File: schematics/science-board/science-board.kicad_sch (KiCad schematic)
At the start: 16 parts, among them J1 Conn_01x02, J10 Conn_01x04, J2 Conn_01x08, J3 Conn_01x04, J4 Conn_01x04, J5 Conn_01x08, J6 Conn_01x03, J7 Conn_01x08, J8 Conn_01x08, J9 Conn_01x04, U1 Teensy4.1, U2 LSF0108PWR

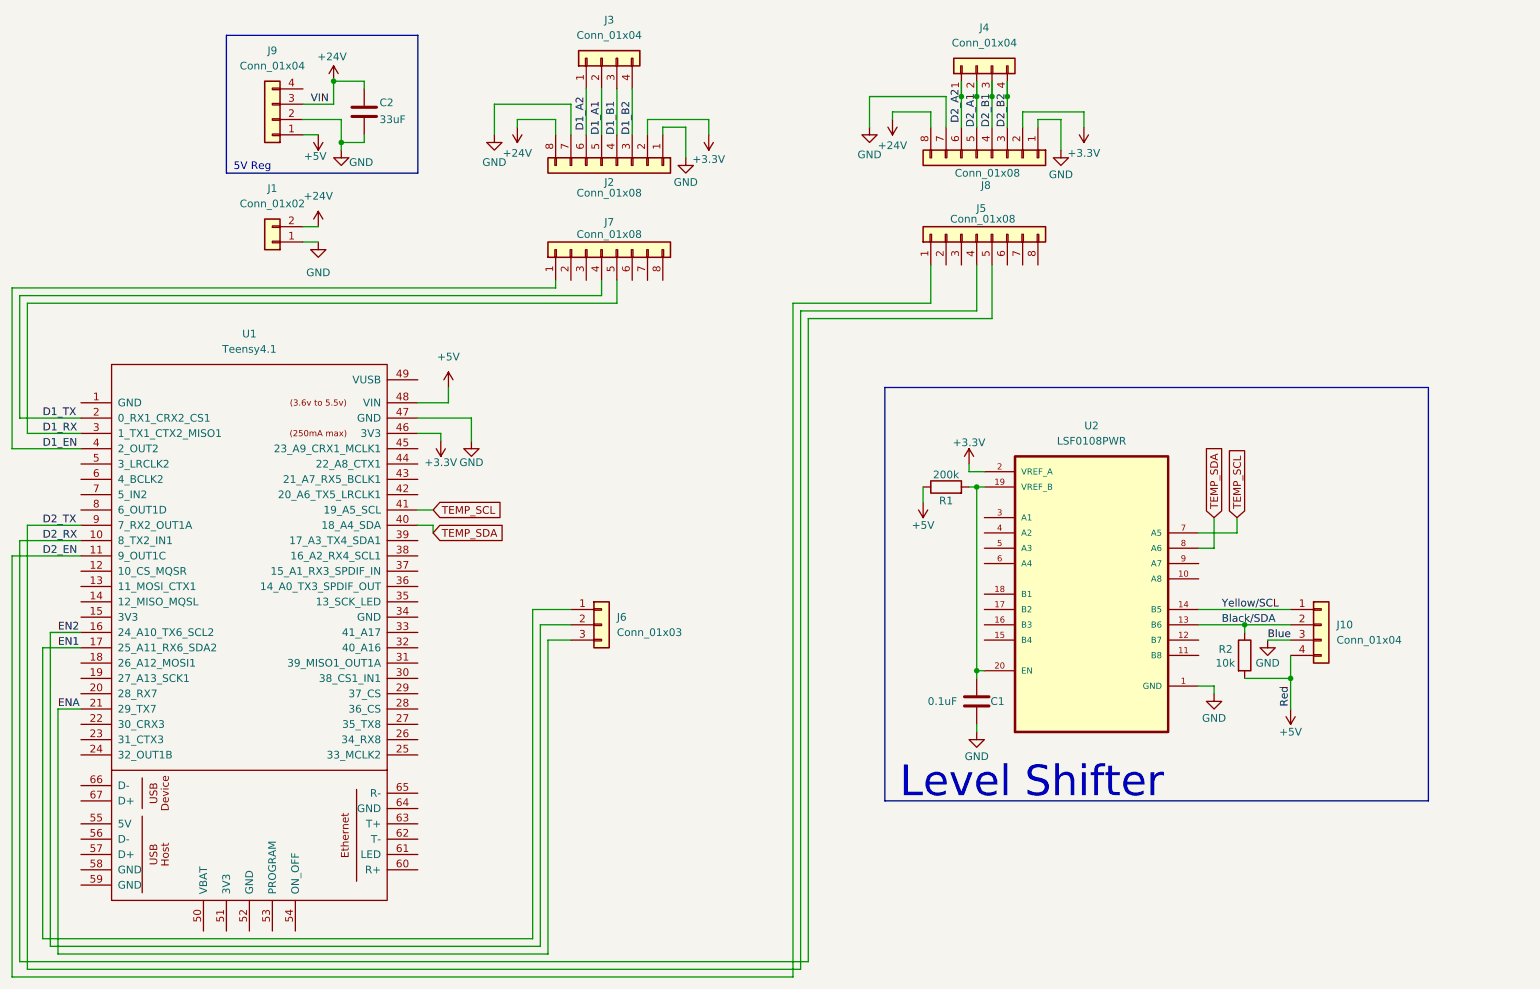
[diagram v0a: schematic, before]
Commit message: Finished preliminary routing. Used through-hole footprints.
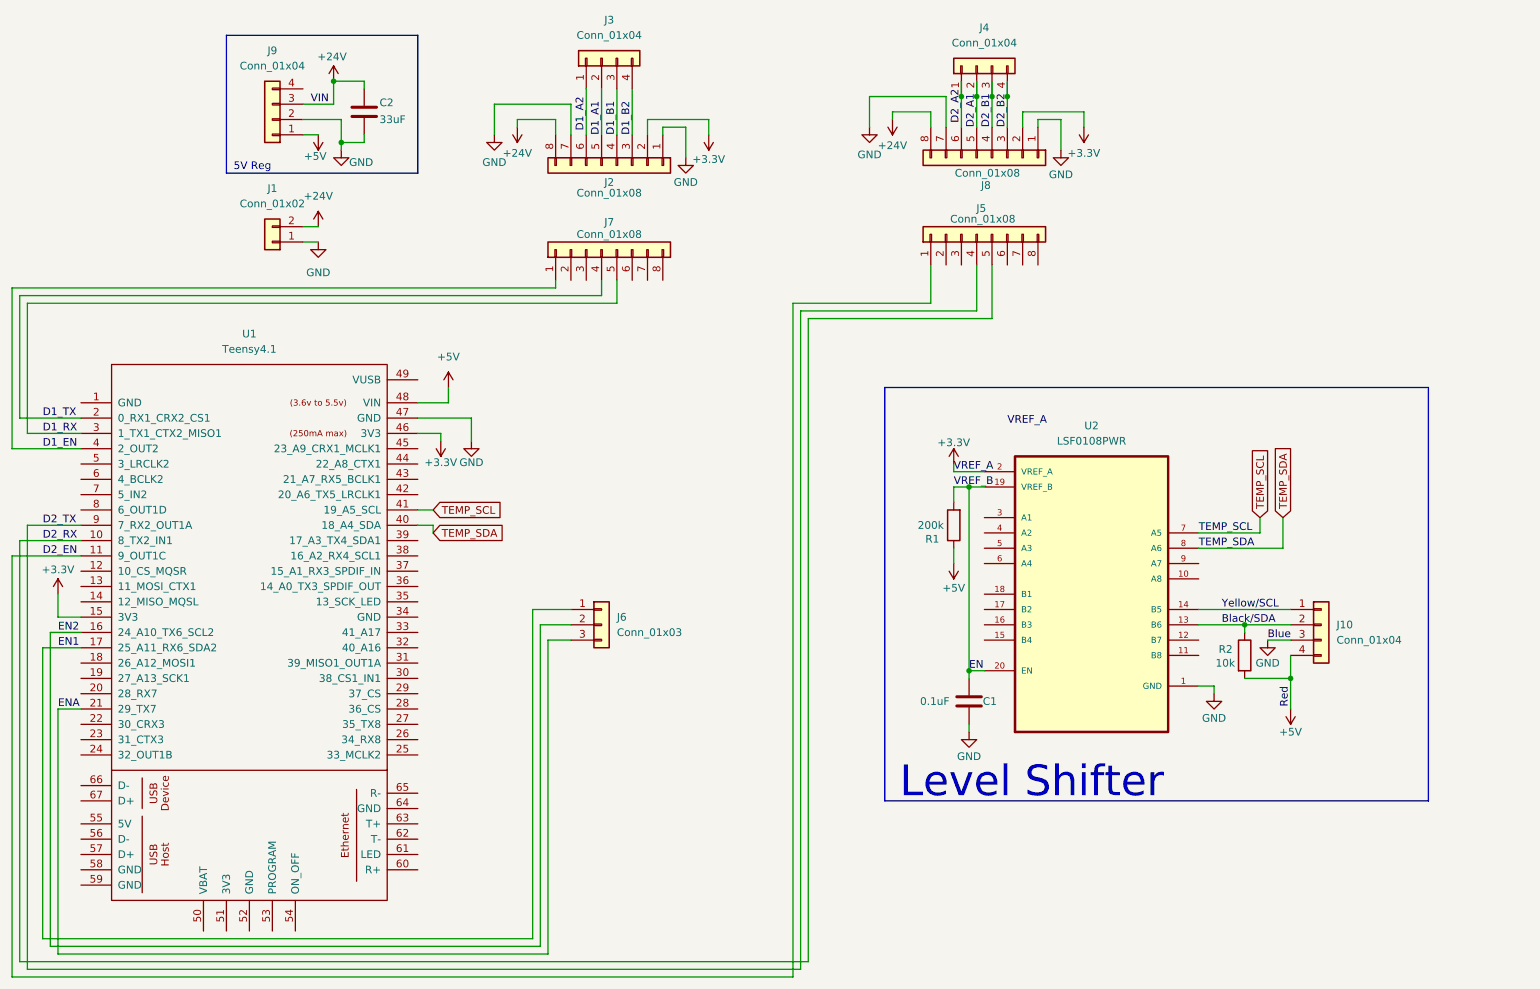
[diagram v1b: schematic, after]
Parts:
- C1: footprint Capacitor_SMD:C_0603_1608Metric -> Capacitor_THT:C_Disc_D3.0mm_W1.6mm_P2.50mm
- C2: footprint Capacitor_SMD:C_0805_2012Metric -> Capacitor_THT:CP_Radial_D4.0mm_P1.50mm
- R1, R2: footprint Resistor_SMD:R_0603_1608Metric -> Resistor_THT:R_Axial_DIN0204_L3.6mm_D1.6mm_P5.08mm_Horizontal
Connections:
- net +3.3V: now also U1.15 (3V3)
- net EN: now reaches C1.1, R1.2, U2.19 (VREF_B), U2.20 (EN)
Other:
- moved on the sheet: C1, R1

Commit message: Added Ethernet module.
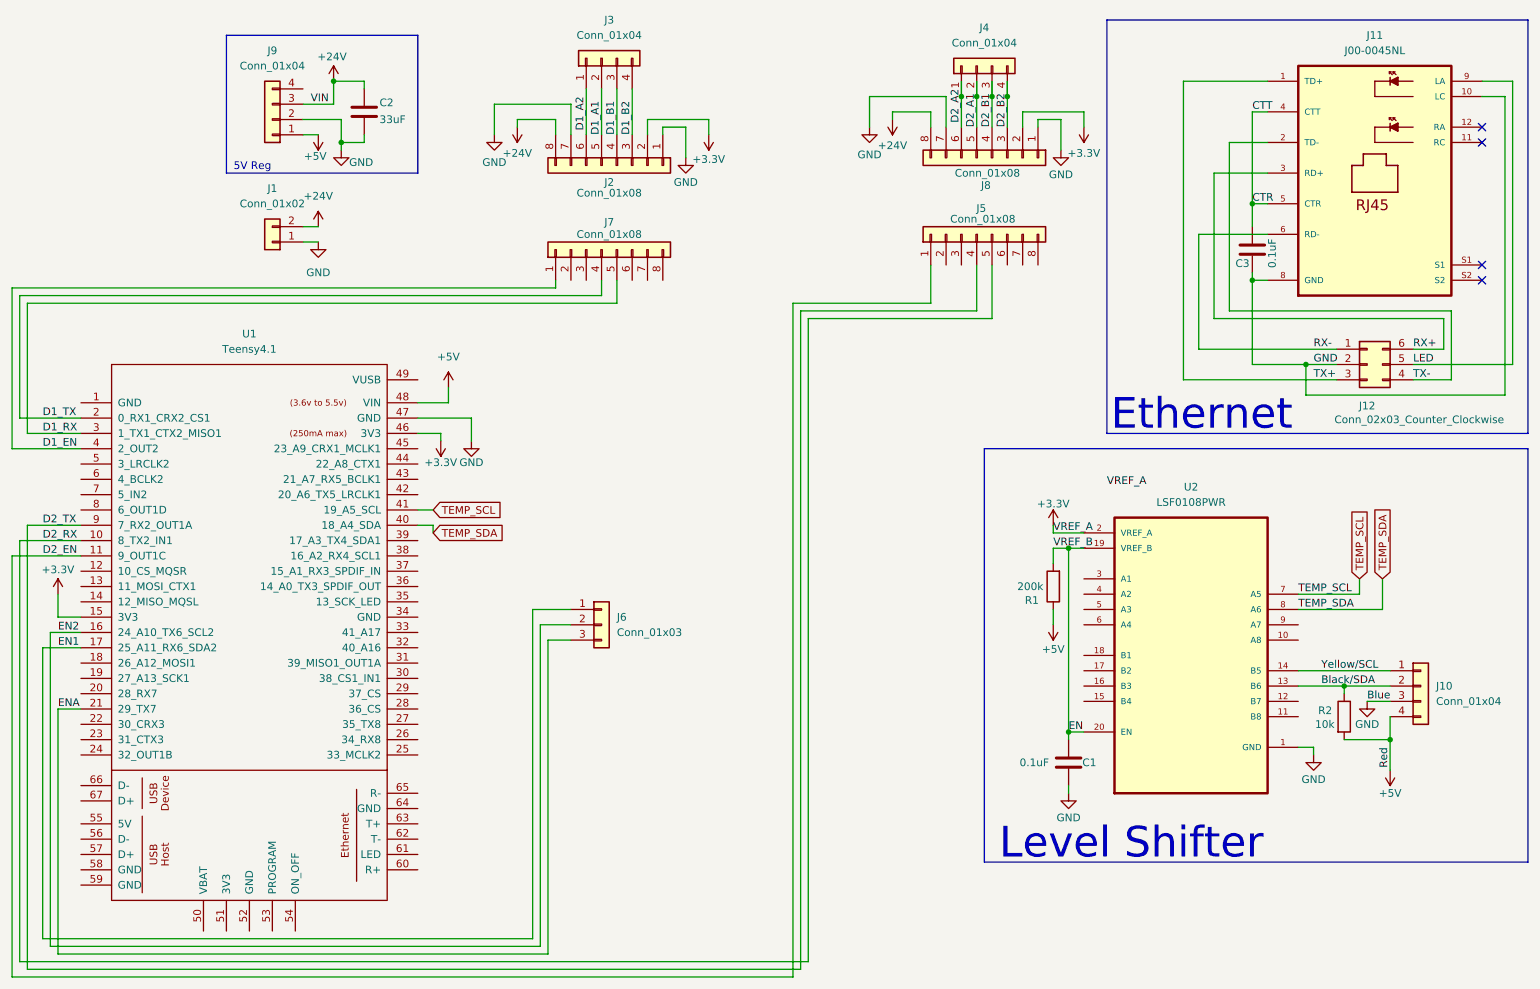
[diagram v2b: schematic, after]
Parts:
- added C3: 0.1uF, Capacitor_THT:C_Disc_D3.0mm_W1.6mm_P2.50mm, symbol Device:C
- added J11: J00-0045NL, J00-0045NL:PULSE_J00-0045NL, symbol J00-0045NL:J00-0045NL
- added J12: Conn_02x03_Counter_Clockwise, Connector_PinHeader_2.00mm:PinHeader_2x03_P2.00mm_Vertical, symbol Connector_Generic:Conn_02x03_Counter_Clockwise
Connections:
- net GND: now also C3.2, J11.10 (LC), J11.8 (GND), J12.2 (Pin_2)
- new net CTR: C3.1, J11.4 (CTT), J11.5 (CTR)
- new net LED: J11.9 (LA), J12.5 (Pin_5)
- new net RX+: J11.3 (RD+), J12.6 (Pin_6)
- new net RX-: J11.6 (RD-), J12.1 (Pin_1)
- new net TX+: J11.1 (TD+), J12.3 (Pin_3)
- new net TX-: J11.2 (TD-), J12.4 (Pin_4)
- no-connect marks 0 -> 4
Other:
- note added: "Ethernet"
- moved on the sheet: C1, J10, R1, R2, U2
